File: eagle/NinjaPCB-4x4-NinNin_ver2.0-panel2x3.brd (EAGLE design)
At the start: 209 x 182 mm, 462 parts, among them IC1 ANALOGSW_AD_SOT23-6, IC10 ANALOGSW_AD_SOT23-6, IC11 NAU7802, IC12 ANALOGSW_AD_SOT23-6, IC2 NAU7802, IC3 NAU7802, IC4 ANALOGSW_AD_SOT23-6, IC5 NAU7802, IC6 ANALOGSW_AD_SOT23-6, IC7 NAU7802, IC8 ANALOGSW_AD_SOT23-6, IC9 NAU7802, Q1 IRLB3813PBF, Q10 CJ2302, Q11 CJ2302, Q12 IRLB3813PBF, Q13 S9013, Q14 S9013, Q15 S9013, Q16 CJ2302, Q17 CJ2302, Q18 IRLB3813PBF, Q19 S9013, Q2 CJ2302, Q20 S9013, Q21 S9013, Q22 CJ2302, Q23 CJ2302, Q24 IRLB3813PBF, Q25 S9013, Q26 S9013, Q27 S9013, Q28 CJ2302, Q29 CJ2302, Q3 CJ2302, Q30 IRLB3813PBF, Q31 S9013, Q32 S9013, Q33 S9013, Q34 CJ2302, Q35 CJ2302, Q36 IRLB3813PBF, Q4 S9013, Q5 S9013, Q6 S9013, Q7 S9013, Q8 S9013, Q9 S9013, T1 TPTP20R, T10 TPTP20R, T11 TPTP20R, T12 TPTP20R, T13 TPTP20R, T14 TPTP20R, T15 TPTP20R, T16 TPTP20R, T17 TPTP20R, T18 TPTP20R, T19 TPTP20R, T2 TPTP20R, T20 TPTP20R, T21 TPTP20R, T22 TPTP20R, T23 TPTP20R, T24 TPTP20R, T25 TPTP20R, T26 TPTP20R, T27 TPTP20R, T28 TPTP20R, T29 TPTP20R, T3 TPTP20R, T30 TPTP20R, T31 TPTP20R, T32 TPTP20R, T33 TPTP20R, T34 TPTP20R, T35 TPTP20R, T36 TPTP20R, T37 TPTP20R, T38 TPTP20R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

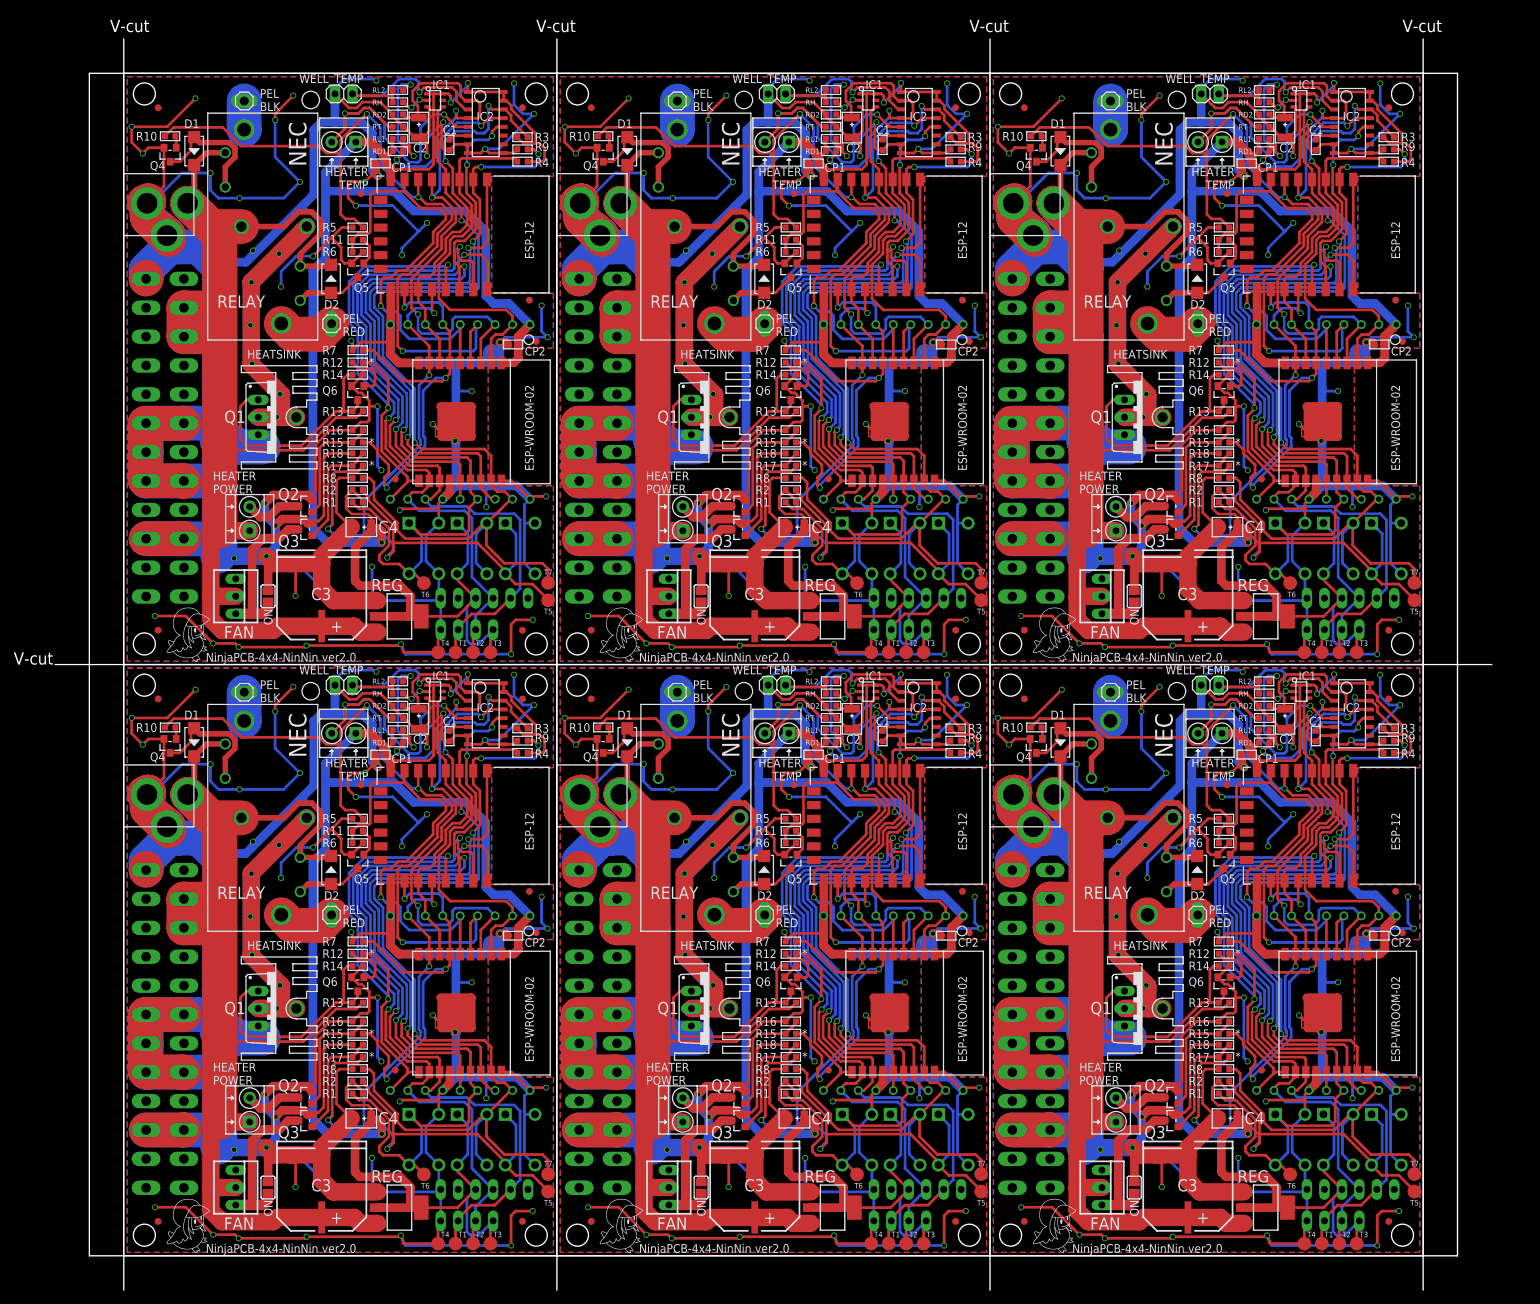
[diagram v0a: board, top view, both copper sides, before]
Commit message: set distance more equal 10mil for 2oz at Seeed
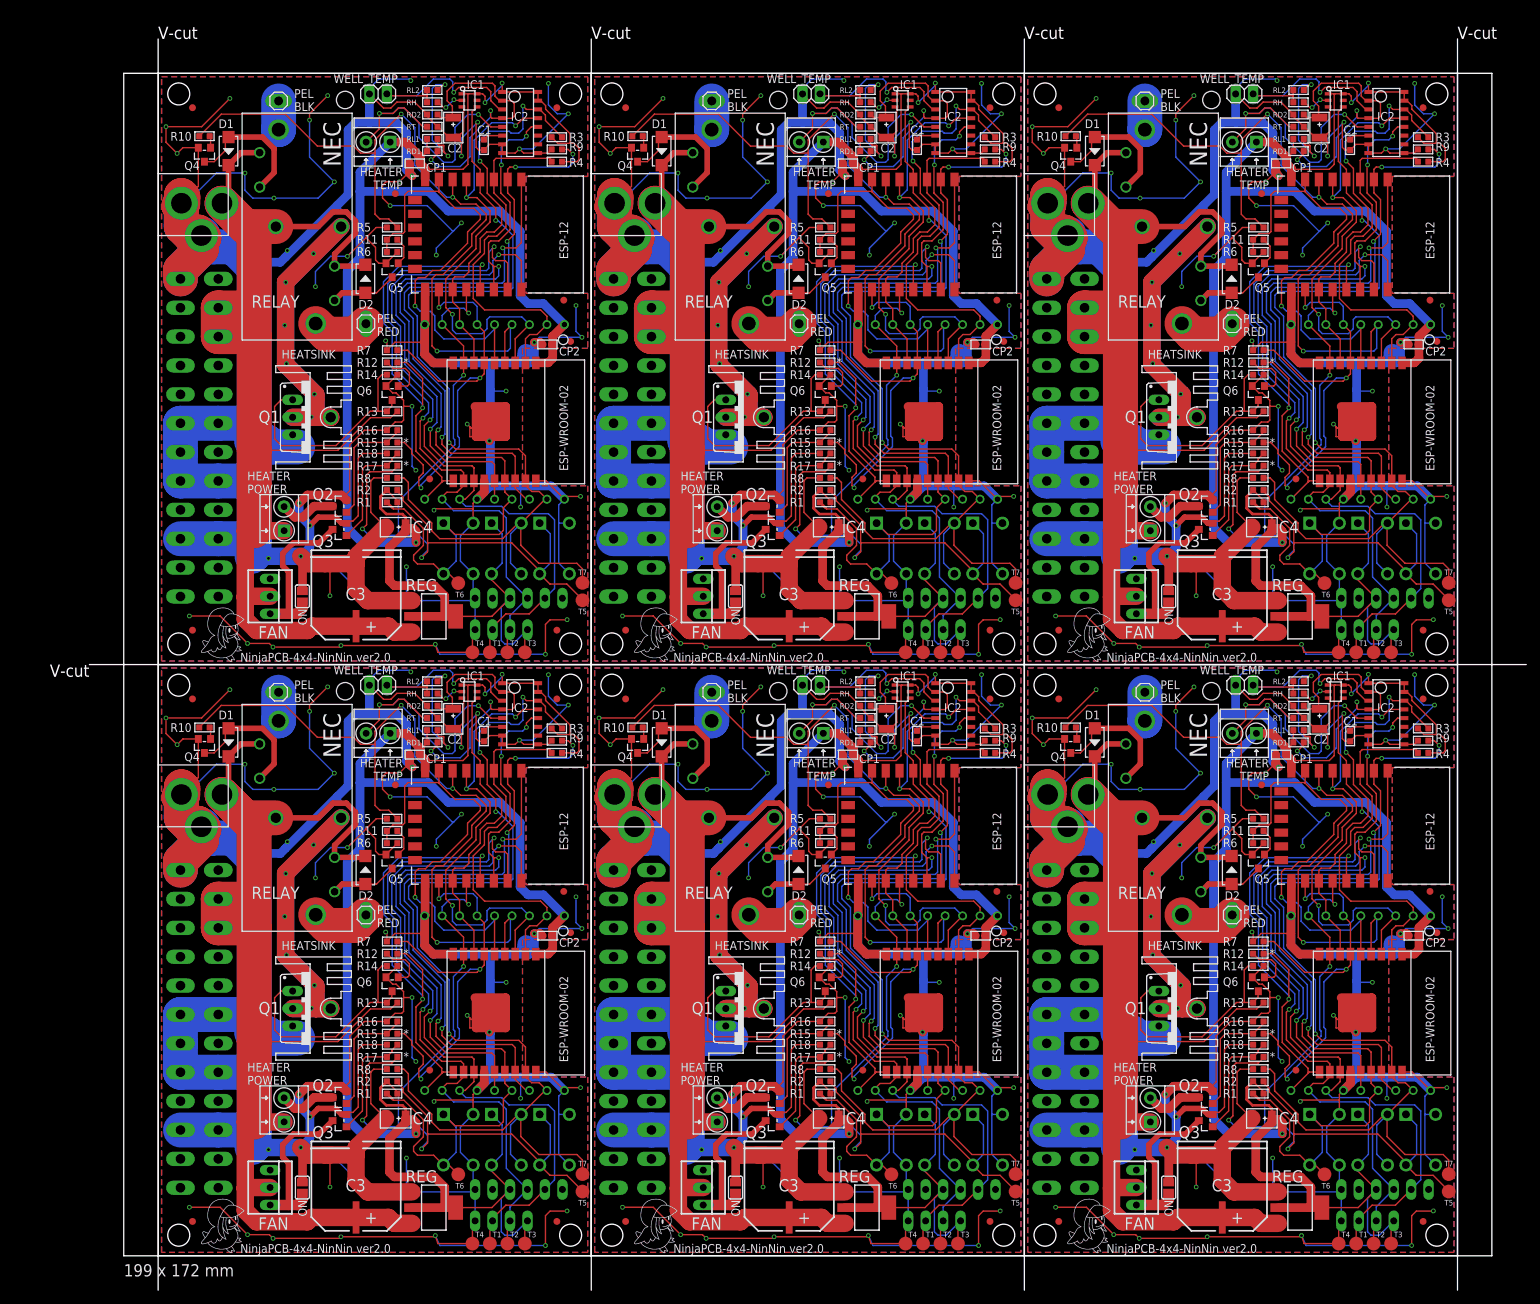
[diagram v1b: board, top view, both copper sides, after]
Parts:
- moved C17 109.6 mm to (165.5, 20.0)
- moved C18 109.6 mm to (159.8, 10.1)
- moved C19 109.6 mm to (178.4, 75.6)
- moved CP10 109.6 mm to (187.6, 46.6)
- moved ESP-4 109.6 mm to (180.4, 62.6)
- moved ESP-WROOM-02-BREAK4 109.6 mm to (179.9, 36.8)
- moved R84 109.6 mm to (137.7, 76.9)
- moved RH4 109.6 mm to (170.9, 81.8)
- moved RL10 109.6 mm to (170.9, 76.5)
- moved T30 109.6 mm to (181.8, 1.78)
- moved T33 109.6 mm to (192.7, 9.35)
- moved T35 109.6 mm to (192.7, 11.9)
- moved ATX4 109.6 mm to (137.0, 33.0)
- moved CP9 109.6 mm to (168.3, 72.9)
- moved D10 109.6 mm to (161.2, 56.1)
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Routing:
- net GND3: track 823.1 -> 809.8 mm
- net GND: track 823.1 -> 809.8 mm
- net GND1: track 823.1 -> 809.8 mm
- net GND5: track 823.1 -> 809.8 mm
- net GND2: track 823.1 -> 809.8 mm
- net GND4: track 823.1 -> 809.8 mm
- net PEL_SWA: track 116.6 -> 118.2 mm
- net PEL_SWA4: track 116.6 -> 118.2 mm
- net PEL_SWA2: track 116.6 -> 118.2 mm
- net PEL_SWA5: track 116.6 -> 118.2 mm
- net PEL_SWA3: track 116.6 -> 118.2 mm
- net PEL_SWA1: track 116.6 -> 118.2 mm
- net N$72: track 18.7 -> 19.6 mm
- net N$33: track 18.7 -> 19.6 mm
- net N$17: track 18.7 -> 19.6 mm
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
